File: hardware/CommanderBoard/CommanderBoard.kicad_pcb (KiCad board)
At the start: 2 copper layers, 63.5 x 106.7 mm, 41 parts, among them J1 Conn_01x22, J1BUS1 Conn_02x04_Odd_Even, J1BUS2 Conn_02x04_Odd_Even, J2 Conn_01x22, J2BUS1 Conn_01x02, J2BUS2 Conn_01x02, J3 HUB75, SW1 SW_SPDT, SW2 SW_DP3T, SW3 SW_DP3T, SW4 SW_DPDT_x2

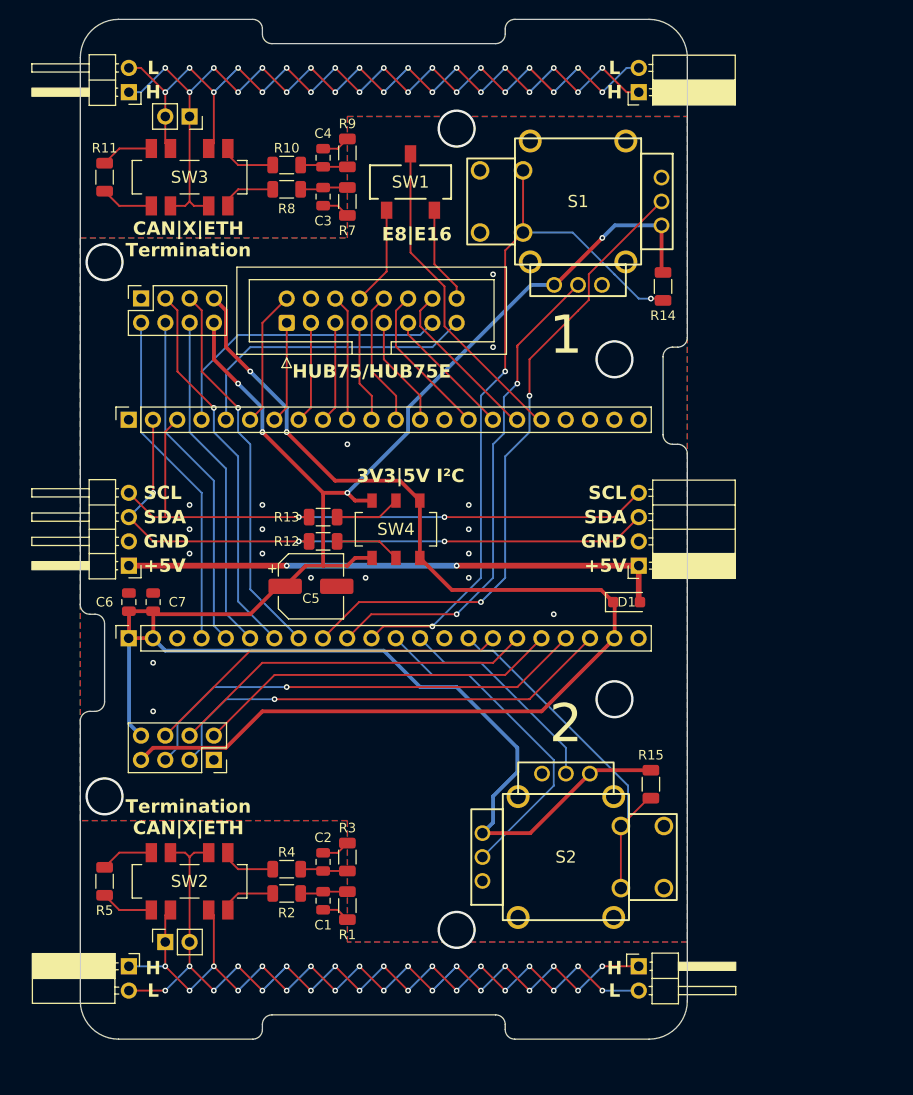
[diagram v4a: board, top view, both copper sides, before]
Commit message: Gave thumbstuck #1 a bit more space.
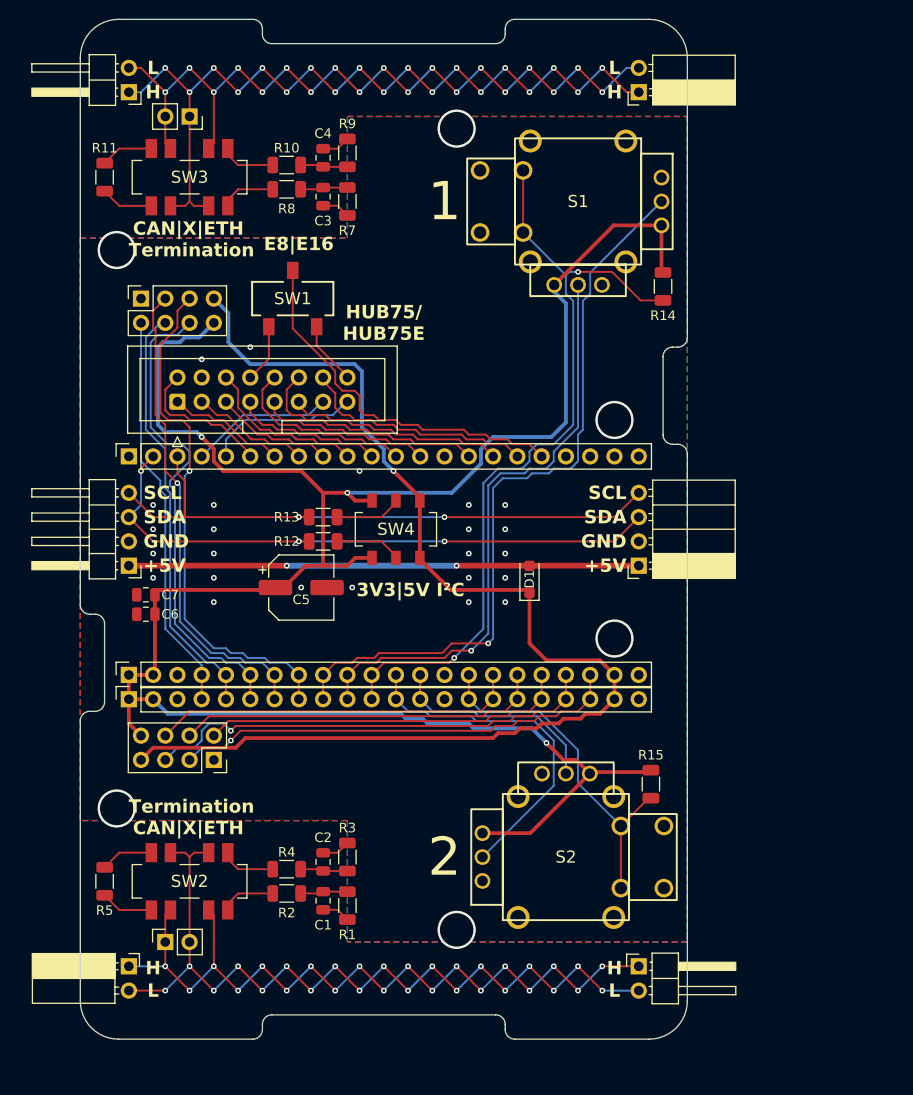
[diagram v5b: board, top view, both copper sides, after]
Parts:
- added J4: Conn_01x22, Connector_PinSocket_2.54mm:PinSocket_1x22_P2.54mm_Vertical, F.Cu at (100.3, 94.0)
- moved SW1 17.3 mm to (117.5, 52.1)
- moved J3 14.1 mm to (105.4, 62.9)
- moved D1 10.4 mm to (142.2, 81.4), turned to 90 degrees
- moved J1 3.84 mm to (100.3, 68.6)
- moved J2 3.84 mm to (100.3, 91.4)
- moved C6 2.18 mm to (102.1, 85.1), turned to 0 degrees
- moved C7 1.08 mm to (102.1, 83.1), turned to 0 degrees
- moved C5 1.02 mm to (118.4, 82.3)
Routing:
- net +3V3: track 206.3 -> 223.7 mm, vias 4 -> 3
- net H75_CLK: track 31.3 -> 15.1 mm
- net H75_OE: track 31.3 -> 16.1 mm
- net CS_N2: track 35.6 -> 50.6 mm
- net TxD2/MISO2: track 40.3 -> 54.1 mm
- net S1vCh: track 67.8 -> 78.5 mm, vias 2 -> 1
- net RxD2/MOSI2: track 40.3 -> 50.2 mm
- net S1hCh: track 52.2 -> 62.0 mm, vias 2 -> 1
- net H75_C: track 13.8 -> 22.9 mm
- net SCLK2: track 35.6 -> 44.4 mm
- net H75_D: track 16.3 -> 25.0 mm
- net BTN1: track 76.1 -> 84.3 mm, vias 3 -> 2
- net H75_LAT: track 17.6 -> 24.9 mm
- net H75_A: track 11.7 -> 18.3 mm
- net IRQ_N2: track 35.6 -> 42.0 mm
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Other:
- board text added: "HUB75/ HUB75E"
- board text removed: "HUB75/HUB75E"

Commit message: Minor improvements.
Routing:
- net +5V: track 125.8 -> 138.2 mm
- net S1vCh: track 78.5 -> 77.5 mm
- net +3V3: track 223.7 -> 222.8 mm
- net GNDREF: vias 30 -> 27

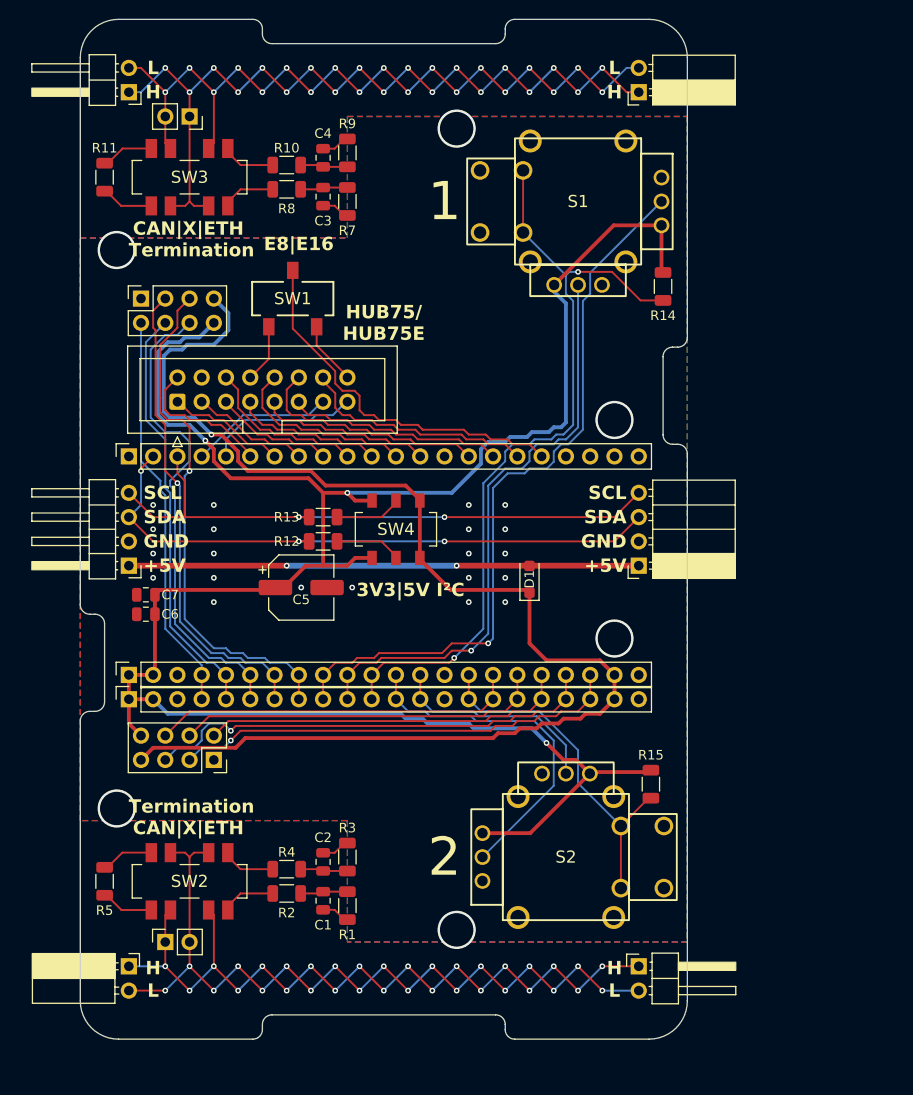
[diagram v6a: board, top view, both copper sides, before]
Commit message: Added I2C passthrough (listener) mode.
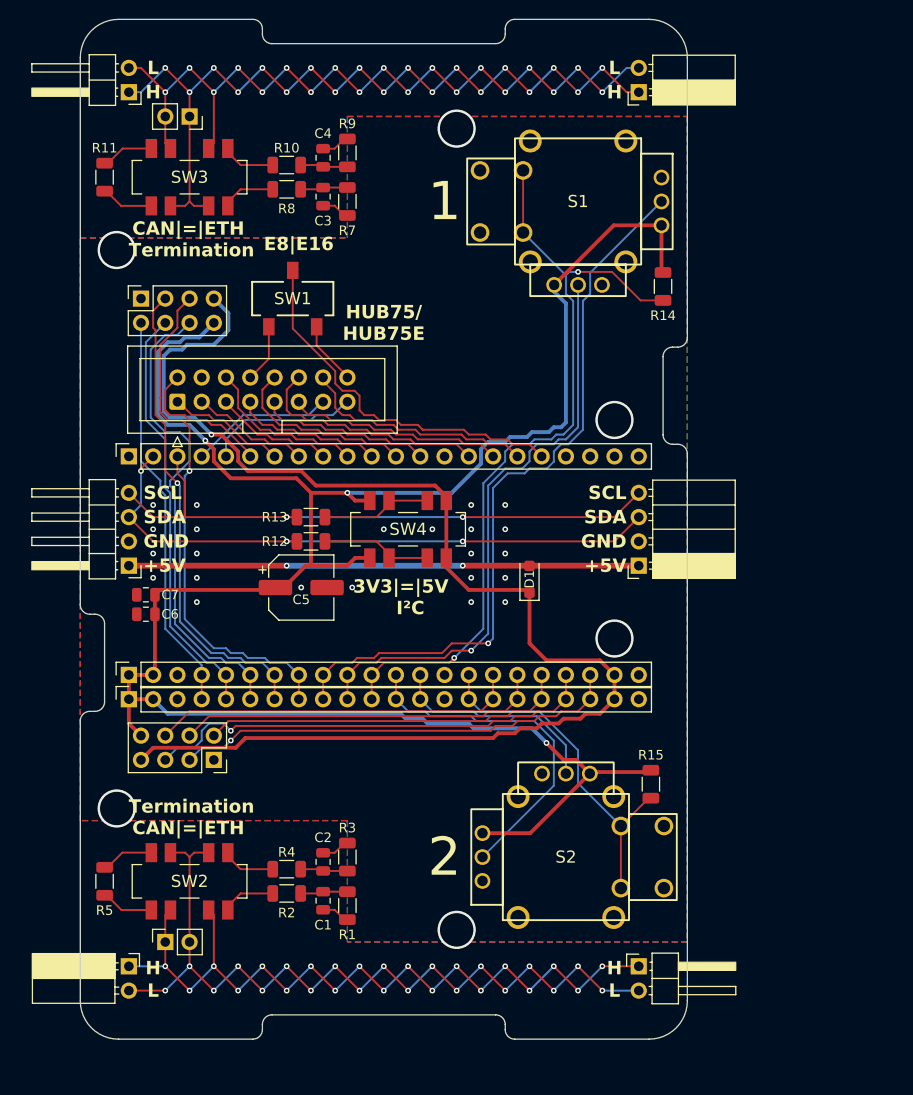
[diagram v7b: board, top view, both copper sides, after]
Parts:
- SW4: value SW_DPDT_x2 -> SW_DP3T; footprint LIB_CL-SB-22B-01T:CLSB22B01T -> LIB_CL-SB-23B-01T:CLSB23B01T
- moved R12 1.27 mm to (119.4, 77.5)
- moved R13 1.27 mm to (119.4, 74.9)
- moved SW4 1.27 mm to (129.5, 76.2)
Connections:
- R12 pad 1: Net-(SW4B-B) -> Net-(R12-Pad1)
- R13 pad 1: Net-(SW4A-B) -> Net-(R13-Pad1)
- SW4 pad 2: Net-(SW4A-B) -> Net-(R13-Pad1)
- SW4 pad 3: +3V3 -> Net-(R13-Pad1)
- SW4 pad 4: +5V -> +3V3
- SW4 pad 5: Net-(SW4B-B) -> +5V
- SW4 pad 6: +3V3 -> Net-(R12-Pad1)
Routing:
- net Net-(R13-Pad1): track 0.00 -> 11.7 mm
- net Net-(R12-Pad1): track 0.00 -> 11.7 mm
- net Net-(SW4A-B): track 7.01 -> 0.00 mm
- net Net-(SW4B-B): track 6.99 -> 0.00 mm
- net +5V: track 138.2 -> 138.9 mm
- net GNDREF: vias 27 -> 29
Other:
- board text added: "3V3|=|5V I²C"
- board text added: "CAN|=|ETH Termination"
- board text added: "Termination CAN|=|ETH"
- board text removed: "3V3|5V I²C"
- board text removed: "CAN|X|ETH Termination"
- board text removed: "Termination CAN|X|ETH"

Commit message: Updated Commanderboard to kicad v10. Added pcis.
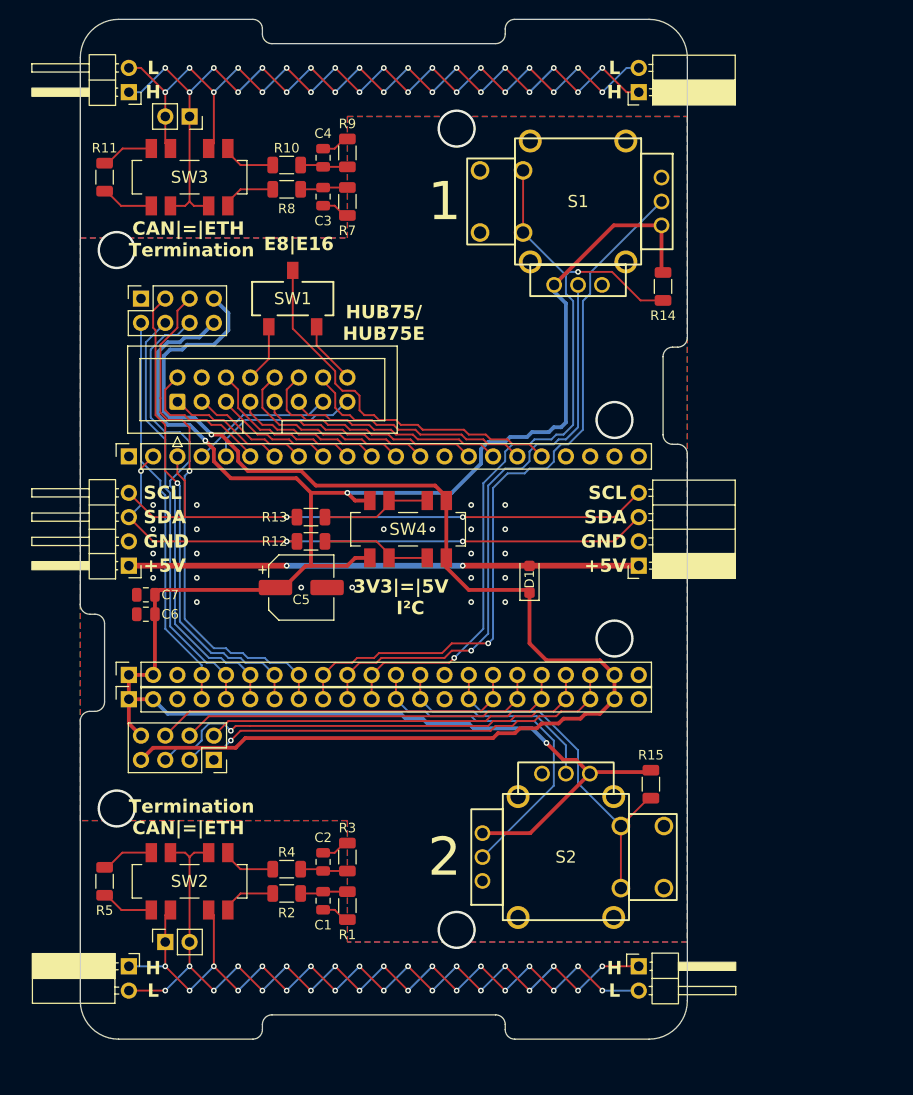
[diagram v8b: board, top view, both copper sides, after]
